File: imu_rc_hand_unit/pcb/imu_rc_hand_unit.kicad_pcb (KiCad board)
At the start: 2 copper layers, 35 x 50 mm, 70 parts, among them J1 USB_C_Receptacle_USB2.0_16P, J2 JST SH1.0, Q1 AO3400A, Q2 AO3400A, Q3 AO3401A, Q4 AO3400A, Q5 AO3401A, Q6 BSS138, SW1 SW_SPDT, U2 MCP73831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

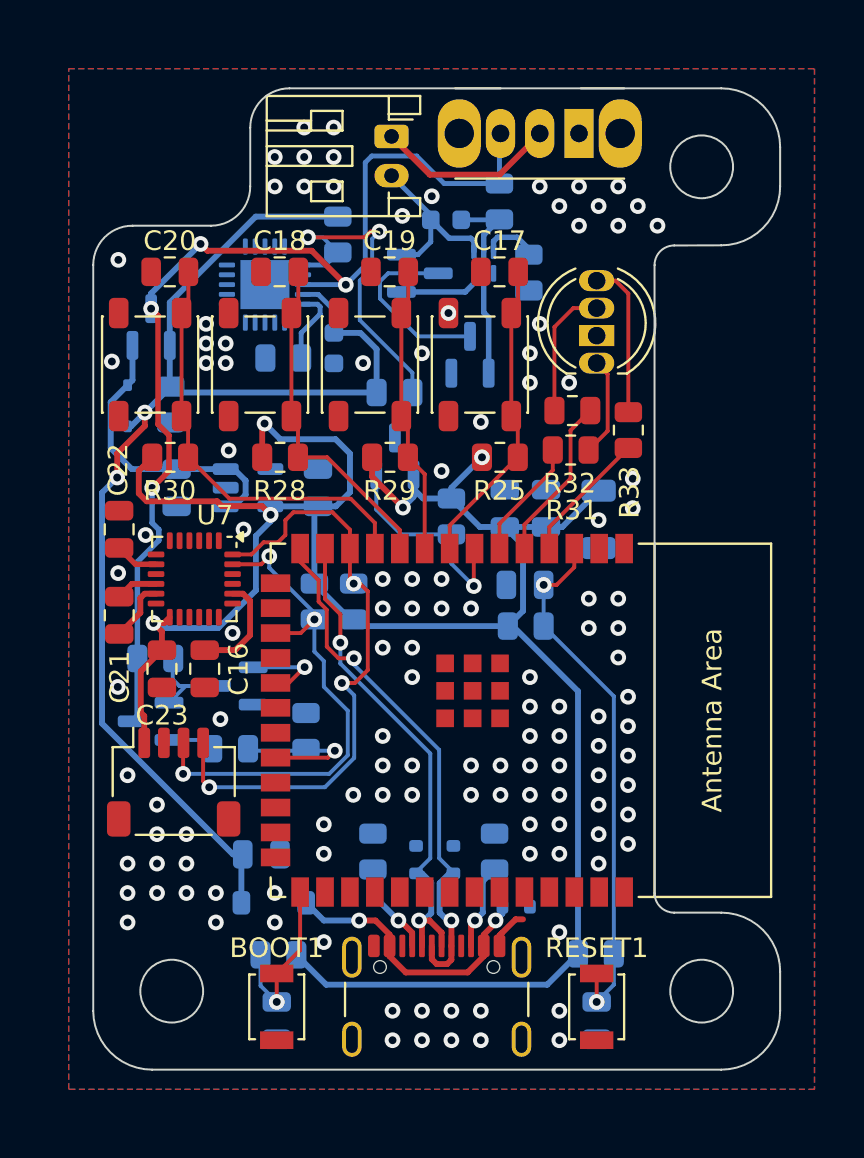
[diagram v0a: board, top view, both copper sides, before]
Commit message: fix DRC errors
Has no errors/warnings now
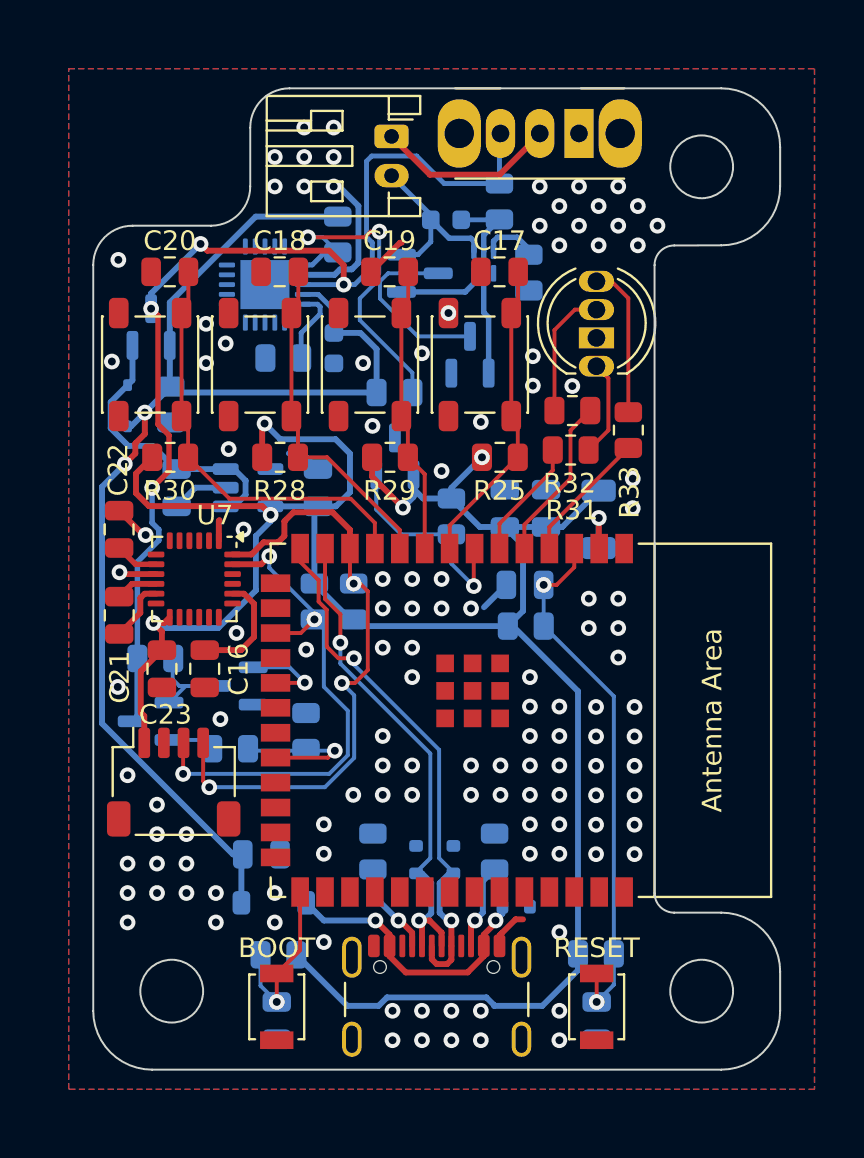
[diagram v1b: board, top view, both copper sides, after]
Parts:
- D7: footprint MyLibrary:LED_D5.0mm-4_RKGB -> IMURCLibrary:LED_D5.0mm-4_RKGB
- renumbered BOOT1 to BOOT, RESET1 to RESET
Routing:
- net GND: track 5.24 -> 26.2 mm
- net Net-(U5-3V3): track 0.00 -> 3.11 mm, vias 0 -> 1
- net +3.3V: track 114.9 -> 116.9 mm
- net +BATT: track 54.0 -> 55.0 mm
- net Net-(D6-K): track 15.2 -> 14.6 mm

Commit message: update pcb text
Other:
- board text added: "ESTG-EEC 24/25"
- board text added: "IMU-RC Hand Unit"
- board text added: "JLCJLCJLCJLC"
- board text added: "v1.0.0"
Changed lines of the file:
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@@
 		(layer "Margin")
+	)
+	(gr_text "JLCJLCJLCJLC"
+		(at 20.67 64.17 -90)
+		(layer "B.SilkS")
+		(effects
+			(font
+				(size 1 1)
+				(thickness 0.15)
+			)
+			(justify left bottom mirror)
+		)
+	)
+	(gr_text "IMU-RC \nHand Unit"
+		(at 48.27 50.29 0)
+		(layer "B.SilkS")
+		(effects
+			(font
+				(size 1 1)
+				(thickness 0.15)
+			)
+			(justify left mirror)
+		)
+	)
+	(gr_text "ESTG-EEC \n24/25"
+		(at 48.2 56.22 0)
+		(layer "B.SilkS")
+		(effects
+			(font
+				(size 1 1)
+				(thickness 0.15)
+			)
+			(justify left bottom mirror)
+		)
+	)
+	(gr_text "v1.0.0"
+		(at 37.84 26.43 -0)
+		(layer "F.SilkS")
+		(effects
+			(font
+				(size 1 1)
+				(thickness 0.15)
+			)
+			(justify left bottom)
+		)
 	)
 	(segment

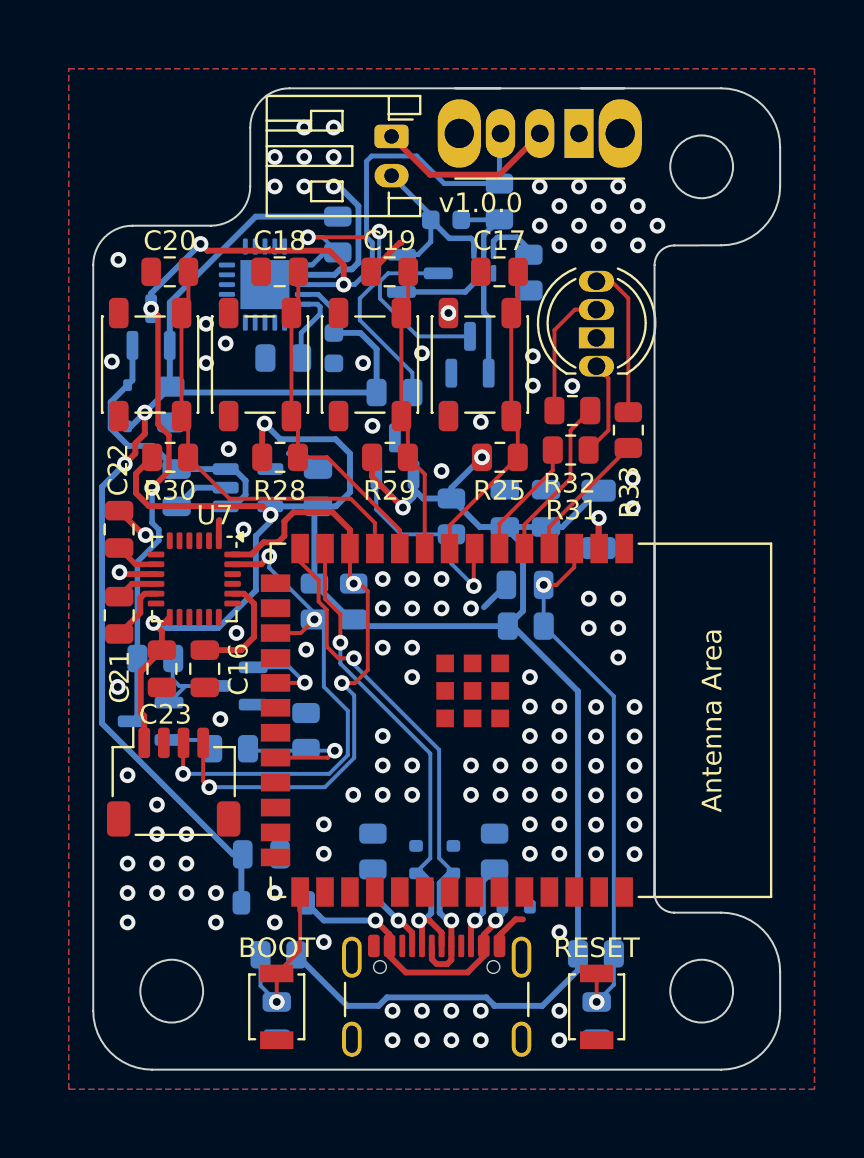
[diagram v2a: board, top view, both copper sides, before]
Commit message: commit #10
created and added LSM6DSO to PCB
Changed MPU to LSM6
Added back UART converter
Added battery reader module
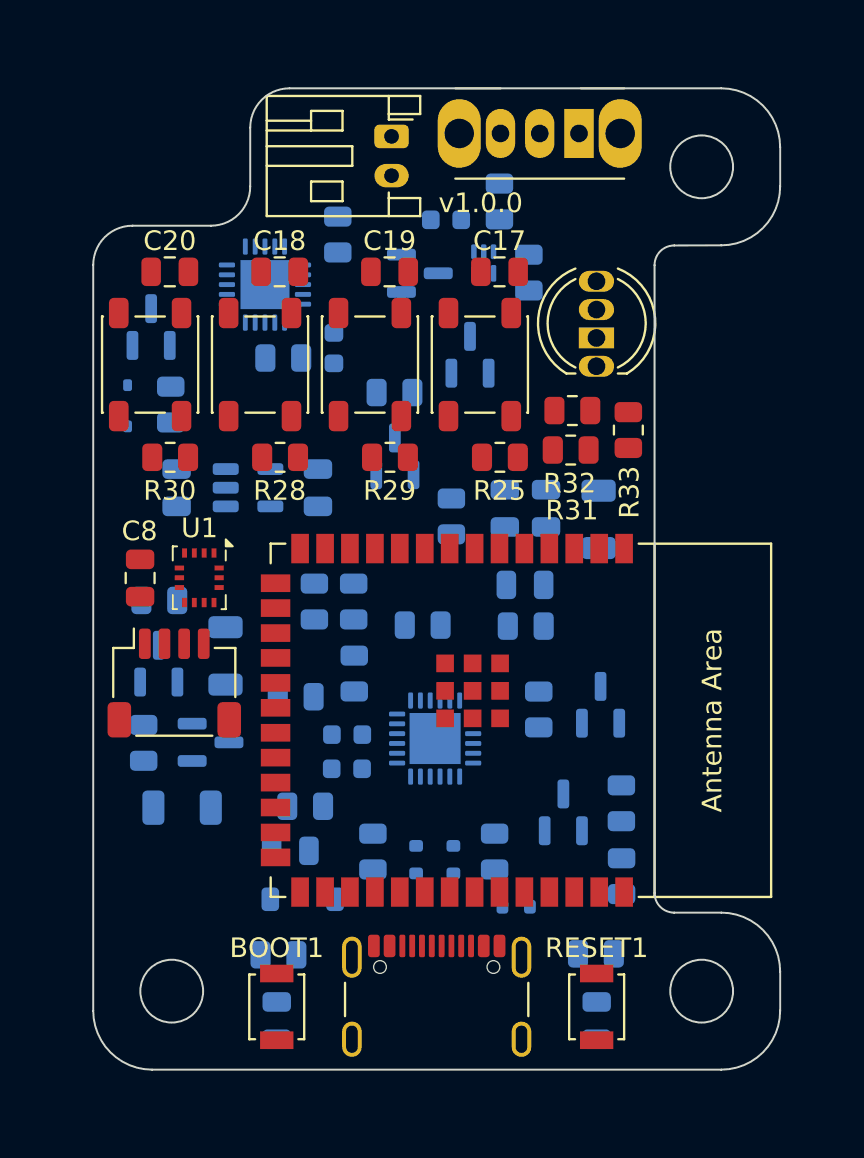
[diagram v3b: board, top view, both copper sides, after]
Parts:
- removed C16: 2n2F/16V, Capacitor_SMD:C_0805_2012Metric
- removed C21, C23: 100nF/16V, Capacitor_SMD:C_0805_2012Metric
- removed C22: 10nF/16V, Capacitor_SMD:C_0805_2012Metric
- removed U7: MPU-6050, Sensor_Motion:InvenSense_QFN-24_4x4mm_P0.5mm
- added C2: 1uF/16V(10%), Capacitor_SMD:C_0603_1608Metric, B.Cu at (33.2, 52.9)
- added C3: 10uF/25V, Capacitor_SMD:C_0603_1608Metric, B.Cu at (33.2, 54.7)
- added C8: 0.1uF/50V(10%), Capacitor_SMD:C_0805_2012Metric, F.Cu at (22.6, 45.0)
- added Q7: 2N2907A, Package_TO_SOT_SMD:SOT-23, B.Cu at (23.6, 49.3)
- added Q8: 2N2907A, Package_TO_SOT_SMD:SOT-23, B.Cu at (26.2, 53.3)
- added R19: 10k, Resistor_SMD:R_0805_2012Metric, B.Cu at (22.8, 53.4)
- added R22: 10k, Resistor_SMD:R_0805_2012Metric, B.Cu at (23.6, 46.1)
- added R23: 0, Resistor_SMD:R_1206_3216Metric, B.Cu at (27.0, 48.9)
- added R24: 0, Resistor_SMD:R_1206_3216Metric, B.Cu at (24.8, 56.7)
- added R3: 22k1, Resistor_SMD:R_0805_2012Metric, B.Cu at (31.0, 56.6)
- added R4: 47k5, Resistor_SMD:R_0805_2012Metric, B.Cu at (30.6, 51.0)
- added R5: 1k, Resistor_SMD:R_0805_2012Metric, B.Cu at (33.5, 49.8)
- added R6: 10k, Resistor_SMD:R_0805_2012Metric, B.Cu at (37.0, 47.4)
- added U1: LSM6DSO, IMURCLibrary:LGA-14L_3x2.5mm_P0.5mm, F.Cu at (25.7, 44.9)
- added U6: CP2102N, Package_DFN_QFN:QFN-24-1EP_4x4mm_P0.5mm_EP2.6x2.6mm, B.Cu at (37.7, 53.1)
- moved Q5 21.5 mm to (44.2, 56.9), turned to 90 degrees
- moved R13 21.0 mm to (47.2, 60.1), turned to 90 degrees
- moved R12 19.7 mm to (43.0, 51.6), turned to -90 degrees
- moved Q4 18.7 mm to (46.1, 51.4), turned to 90 degrees
- moved R14 16.5 mm to (47.2, 56.4)
- moved J2 5.05 mm to (24.4, 50.3)
- moved C1 1.48 mm to (30.3, 58.9)
- moved D4 1.48 mm to (30.9, 61.3)
- renumbered BOOT to BOOT1, RESET to RESET1
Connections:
- D2 pad 2: DN -> Net-(D2-A2)
- D3 pad 2: DP -> Net-(D3-A2)
- J1 pad A6: DP -> Net-(D3-A2)
- J1 pad A7: DN -> Net-(D2-A2)
- J1 pad B6: DP -> Net-(D3-A2)
- J1 pad B7: DN -> Net-(D2-A2)
- U5 pad 13: DN -> unconnected-(U5-GPIO19/U1RTS/ADC2_CH8/CLK_OUT2/USB_D--Pad13)
- U5 pad 14: DP -> unconnected-(U5-GPIO20/U1CTS/ADC2_CH9/CLK_OUT1/USB_D+-Pad14)
- U5 pad 36: unconnected-(U5-U0RXD/GPIO44/CLK_OUT2-Pad36) -> U0RXD
- U5 pad 37: unconnected-(U5-U0TXD/GPIO43/CLK_OUT1-Pad37) -> U0TXD
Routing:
- net +3.3V: track 116.9 -> 0.00 mm, vias 5 -> 0
- net VBUS: track 65.3 -> 0.00 mm, vias 2 -> 0
- net +BATT: track 55.0 -> 0.00 mm, vias 4 -> 0
- net SDA: track 31.5 -> 0.00 mm, vias 3 -> 0
- net CHIP_PU: track 27.4 -> 0.00 mm, vias 2 -> 0
- net DP: track 27.3 -> 0.00 mm, vias 2 -> 0
- net SCL: track 26.5 -> 0.00 mm, vias 3 -> 0
- net GND: track 26.2 -> 0.00 mm, vias 124 -> 0
- net DN: track 25.8 -> 0.00 mm, vias 2 -> 0
- net SW_DOWN: track 21.9 -> 0.00 mm
- net CHRG_5V: track 20.0 -> 0.00 mm, vias 2 -> 0
- net SW_SLT: track 17.4 -> 0.00 mm
- net SW_FN: track 15.8 -> 0.00 mm
- net SW_UP: track 14.7 -> 0.00 mm
- net Net-(D6-K): track 14.6 -> 0.00 mm
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- removed copper zone on B.Cu, net GND
- removed copper zone on F.Cu, net GND

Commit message: commit #12
added cost prevision table #2
minor changes overall
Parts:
- moved R19 23.3 mm to (46.0, 55.0), turned to 0 degrees
- moved Q7 22.6 mm to (46.1, 51.9), turned to -90 degrees
- moved Q4 20.5 mm to (26.1, 46.8)
- moved Q5 20.5 mm to (24.2, 52.3)
- moved R12 20.5 mm to (22.9, 47.0)
- moved R13 20.5 mm to (27.2, 55.5)
- moved R14 20.5 mm to (27.1, 51.8)
- moved Q8 20.4 mm to (46.1, 58.1), turned to -90 degrees
- moved R23 19.1 mm to (46.0, 46.9)
- moved R22 19.0 mm to (42.3, 49.6)
- moved R24 17.1 mm to (37.7, 67.8)
- moved R25 9.60 mm to (41.0, 29.2)
- moved R28 9.60 mm to (29.8, 29.2)
- moved R29 9.60 mm to (35.4, 29.2)
- moved R30 9.60 mm to (24.2, 29.2)
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- renumbered BOOT1 to BOOT, RESET1 to RESET
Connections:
- U5 pad 19: BATT_READ_EN -> unconnected-(U5-GPIO11/TOUCH11/ADC2_CH0/FSPID/FSPIIO5/SUBSPID-Pad19)
- U5 pad 23: unconnected-(U5-GPIO21-Pad23) -> BATT_READ_EN
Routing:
- net +3.3V: track 0.00 -> 126.1 mm, vias 0 -> 3
- net +BATT: track 0.00 -> 97.9 mm, vias 0 -> 2
- net VBUS: track 0.00 -> 74.5 mm
- net CHIP_PU: track 0.00 -> 41.4 mm, vias 0 -> 2
- net SW_DOWN: track 0.00 -> 21.8 mm
- net SDA: track 0.00 -> 18.7 mm, vias 0 -> 1
- net SW_SLT: track 0.00 -> 17.6 mm
- net SW_FN: track 0.00 -> 17.2 mm
- net SCL: track 0.00 -> 16.5 mm, vias 0 -> 1
- net Net-(Q8-B): track 0.00 -> 16.4 mm
- net BOOT: track 0.00 -> 16.0 mm, vias 0 -> 1
- net Net-(Q8-C): track 0.00 -> 15.9 mm
- net SW_UP: track 0.00 -> 15.6 mm
- net CHRG_5V: track 0.00 -> 13.8 mm, vias 0 -> 2
- net RTS: track 0.00 -> 13.8 mm
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- added copper zone on B.Cu, net GND
- added copper zone on F.Cu, net GND
